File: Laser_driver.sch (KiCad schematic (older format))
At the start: 1 part

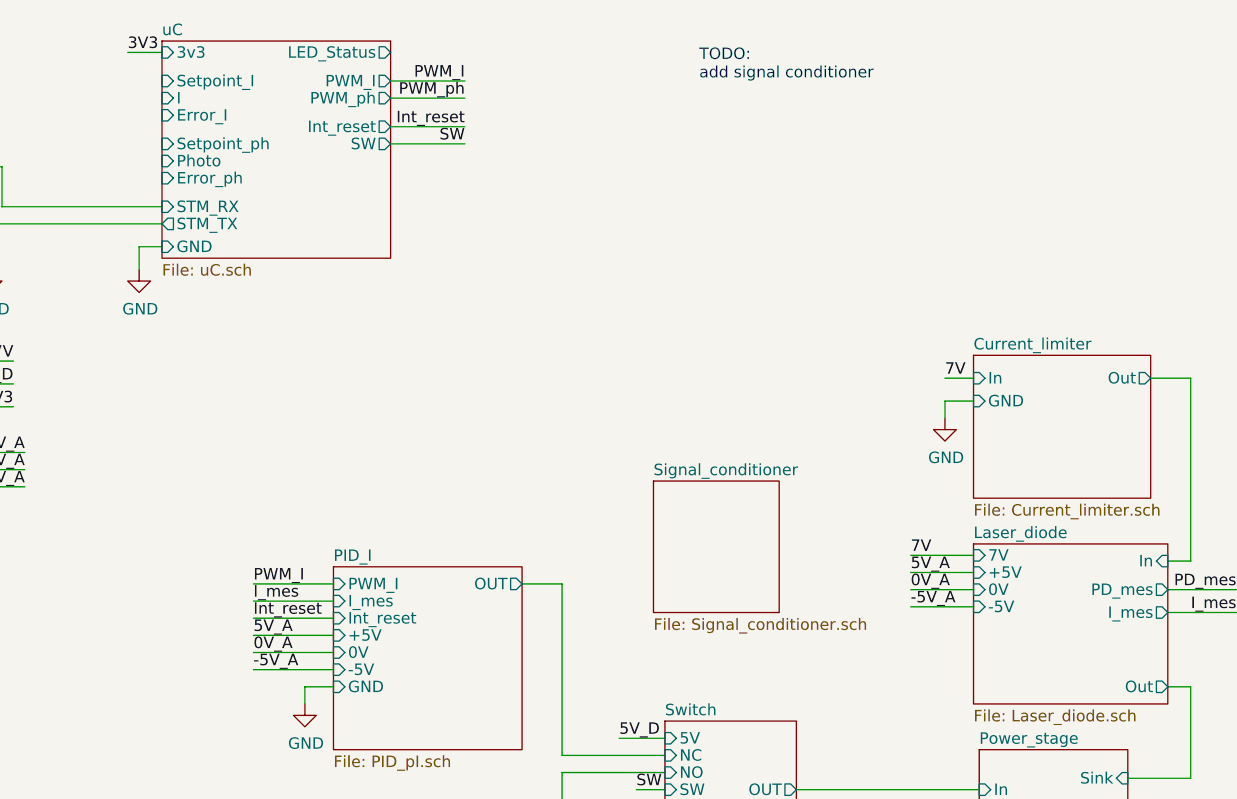
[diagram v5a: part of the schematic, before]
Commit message: Removed uC setpoint measurements
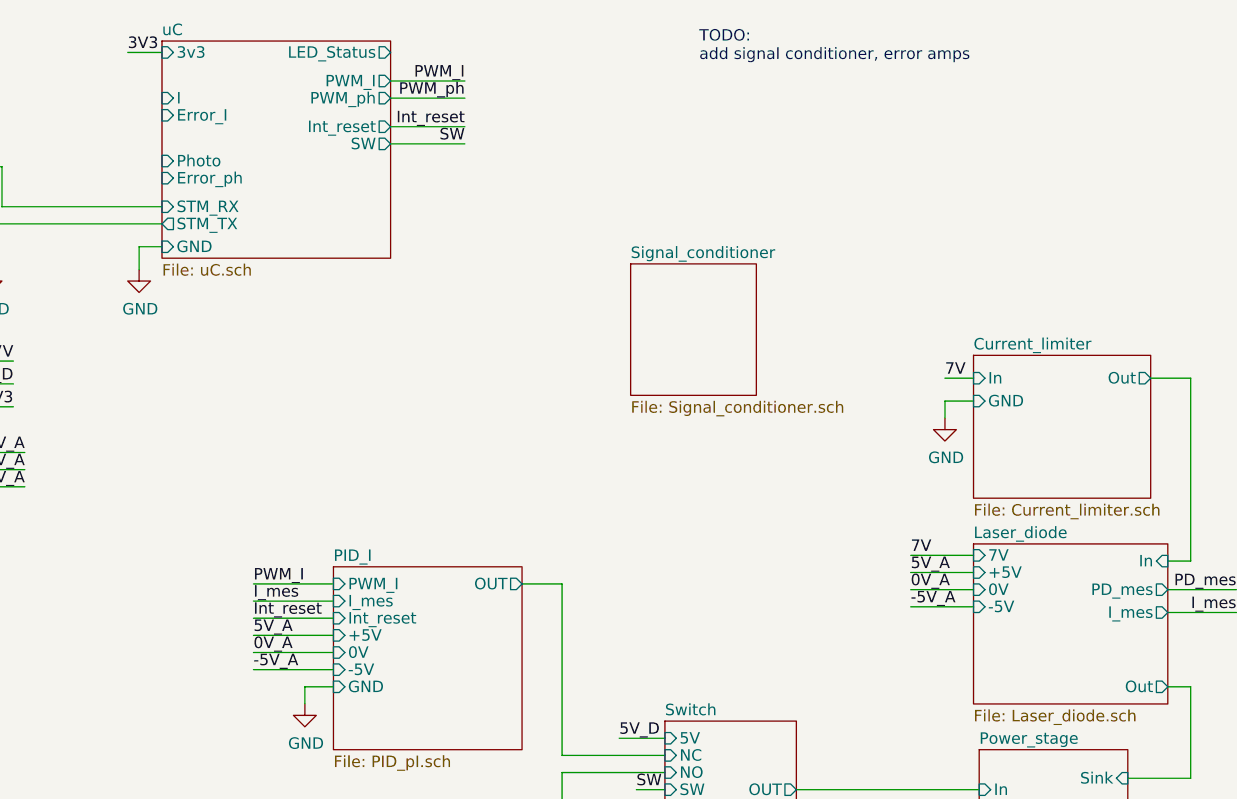
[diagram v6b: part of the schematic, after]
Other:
- note added: "TODO:\nadd signal conditioner, error amps\n\n"
- note removed: "TODO:\nadd signal conditioner\n"
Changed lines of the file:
@@
-$EndSheet
-$Sheet
-S 3150 1125 1000 950
-U 617D45B9
-F0 "uC" 50
-F1 "uC.sch" 50
-F2 "3v3" I L 3150 1175 50
-F3 "Setpoint_I" I L 3150 1300 50
-F4 "I" I L 3150 1375 50
-F5 "Error_I" I L 3150 1450 50
-F6 "Setpoint_ph" I L 3150 1575 50
-F7 "Photo" I L 3150 1650 50
-F8 "Error_ph" I L 3150 1725 50
-F9 "GND" I L 3150 2025 50
-F10 "SW" O R 4150 1575 50
-F11 "PWM_I" O R 4150 1300 50
-F12 "PWM_ph" O R 4150 1375 50
-F13 "Int_reset" O R 4150 1500 50
-F14 "STM_RX" I L 3150 1850 50
-F15 "STM_TX" O L 3150 1925 50
-F16 "LED_Status" O R 4150 1175 50
 $EndSheet
 $Sheet
@@
 $EndSheet
 $Sheet
-S 5300 3050 550  575
+S 5200 2100 550  575
 U 61838F34
 F0 "Signal_conditioner" 50
@@
 -5V_A
 Text Notes 5500 1300 0    50   ~ 0
-TODO:\nadd signal conditioner\n
+TODO:\nadd signal conditioner, error amps\n\n
 Text Label 4475 1500 2    50   ~ 0
 Int_reset
@@
 Text Label 3550 3575 0    50   ~ 0
 I_mes
+$Sheet
+S 3150 1125 1000 950
+U 617D45B9
+F0 "uC" 50
+F1 "uC.sch" 50
+F2 "3v3" I L 3150 1175 50
+F3 "I" I L 3150 1375 50
+F4 "Error_I" I L 3150 1450 50
+F5 "Photo" I L 3150 1650 50
+F6 "Error_ph" I L 3150 1725 50
+F7 "GND" I L 3150 2025 50
+F8 "SW" O R 4150 1575 50
+F9 "PWM_I" O R 4150 1300 50
+F10 "PWM_ph" O R 4150 1375 50
+F11 "Int_reset" O R 4150 1500 50
+F12 "STM_RX" I L 3150 1850 50
+F13 "STM_TX" O L 3150 1925 50
+F14 "LED_Status" O R 4150 1175 50
+$EndSheet
 $EndSCHEMATC
